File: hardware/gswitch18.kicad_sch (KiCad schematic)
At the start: 21 parts, among them IC1 ATMEGA88P, P1 CONN_6X2, P2 CONN_6X2, P3 CONN_6X2, P4 USB, P5 ISP, X1 12MHz

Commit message: v1.2 KiCAD 6 final changes
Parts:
- removed C2: 22u, symbol gswitch18-rescue:CAPAPOL
- added C1: 0u1, Capacitor_SMD:C_0603_1608Metric, symbol gswitch18-rescue:C
- added C5: (no value), symbol gswitch18-rescue:CAPAPOL
- added MH1, MH2, MH3, MH4: (no value), symbol Mechanical:MountingHole
- C2: renamed from C1; footprint (none) -> Capacitor_SMD:C_0603_1608Metric
- C3, C4: footprint (none) -> Capacitor_SMD:C_0603_1608Metric
- D1: footprint (none) -> Diode_SMD:D_SOD-523
- D2: value Sctky -> (none)
- D3, D4: value 3.6v Zen -> (none); footprint (none) -> Capacitor_SMD:C_1206_3216Metric_Pad1.33x1.80mm_HandSolder
- P1, P2, P3: footprint (none) -> pin_array_6x2
- P4: footprint (none) -> USB-B_mini
- P5: footprint (none) -> pin_array_3x2
- R1, R2, R3, R5, R6, R7: footprint (none) -> Resistor_SMD:R_0603_1608Metric
- U1: renamed from IC1; footprint (none) -> Package_QFP:TQFP-32_7x7mm_P0.8mm
- X1: footprint (none) -> HC-49V
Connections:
- net +5V: now also C1.1, C5.1
- net GND: now also D1.2 (A), D2.2 (A), C1.2, C5.2; no longer D1.1 (A), D2.1 (A)
- net at D3.2 (K), R2.1, R3.2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: now also D2.1 (K); no longer D2.2 (K)
- net at D4.2 (K), R1.1, R5.2: now also D1.1 (K); no longer D1.2 (K)
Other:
- moved on the sheet: C2, D1, D2, D3, D4, R1, R2, R3, R5, R6

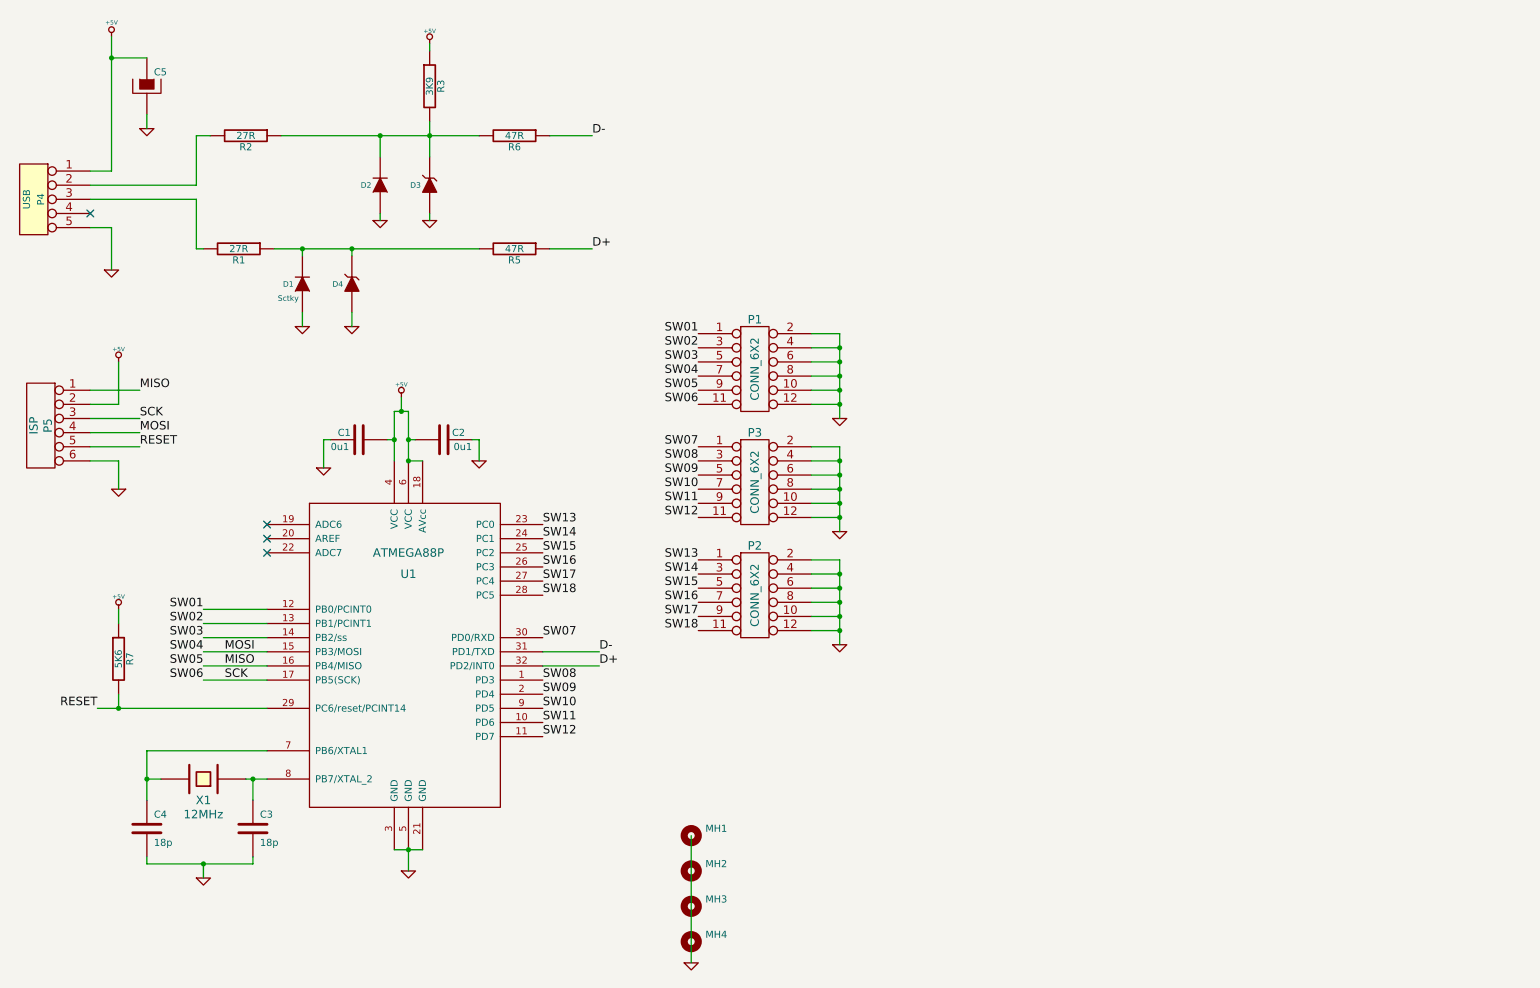
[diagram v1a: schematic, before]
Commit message: Futzing with fully SMD version. Don't like the JST PA connectors.
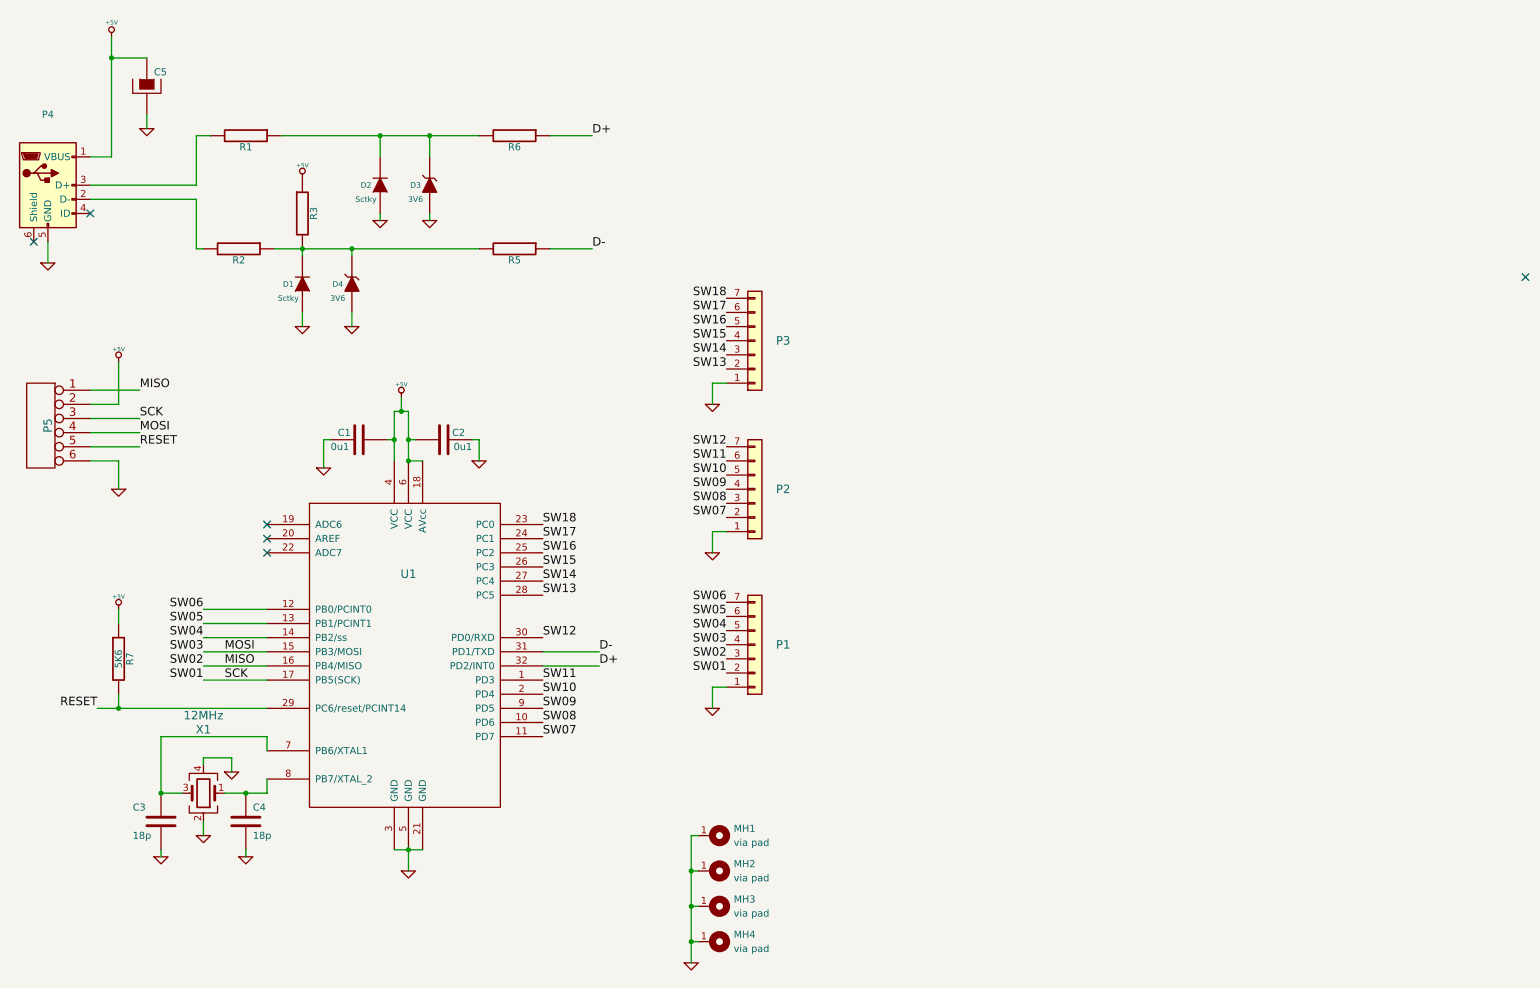
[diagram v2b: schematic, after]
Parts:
- removed P2, P3: CONN_6X2, pin_array_6x2, symbol gswitch18-rescue:CONN_6X2
- removed P4: USB, USB-B_mini, symbol gswitch18-rescue:CONN_5
- added P2, P3: (no value), symbol Connector_Generic:Conn_01x07
- added P4: (no value), symbol Connector:USB_B_Mini
- C5: JLCPCB (none) -> C128254
- D1: JLCPSB (none) -> C122862
- D2: value (none) -> Sctky; footprint (none) -> Diode_SMD:D_SOD-523; JLCPCB (none) -> C122862
- D3, D4: value (none) -> 3V6; footprint Capacitor_SMD:C_1206_3216Metric_Pad1.33x1.80mm_HandSolder -> Diode_SMD:D_SOD-123; JLCPCB (none) -> C8057
- MH1, MH2, MH3, MH4: value (none) -> via pad; footprint (none) -> MountingHole:MountingHole_3.2mm_M3_Pad_Via
- P1: value CONN_6X2 -> (none); footprint pin_array_6x2 -> (none); symbol gswitch18-rescue:CONN_6X2 -> Connector_Generic:Conn_01x07; JLCPCB (none) -> C519164
- P5: value ISP -> (none); footprint pin_array_3x2 -> (none); now left out of the parts list
- R1: renamed from R2; value 27R -> (none); footprint Resistor_SMD:R_0603_1608Metric -> (none); JLCPCB (none) -> C137753
- R2: renamed from R1; value 27R -> (none); footprint Resistor_SMD:R_0603_1608Metric -> (none); JLCPCB (none) -> C137753
- R3: value 3K9 -> (none); footprint Resistor_SMD:R_0603_1608Metric -> (none); JLCPCB (none) -> C137629
- R5, R6: value 47R -> (none); footprint Resistor_SMD:R_0603_1608Metric -> (none); JLCPCB (none) -> C114623
- U1: value ATMEGA88P -> (none); footprint Package_QFP:TQFP-32_7x7mm_P0.8mm -> (none); JLCPCB (none) -> C8727
- X1: footprint HC-49V -> Crystal:Crystal_SMD_3225-4Pin_3.2x2.5mm; symbol gswitch18-rescue:CRYSTAL -> Device:Crystal_GND24; JLCPCB (none) -> C258939
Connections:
- net +5V: now also P4.1 (VBUS)
- net D+: now also R6.1; no longer R5.1
- net D-: now also R5.1; no longer R6.1
- net GND: now also D1.1 (A), D2.1 (A), MH1.1 (G), MH2.1 (G), MH3.1 (G), MH4.1 (G), P1.1 (Pin_1), X1.2, X1.4, P2.1 (Pin_1), P3.1 (Pin_1), P4.5 (GND); no longer D1.2 (A), D2.2 (A), P1.10, P1.12, P1.2 (P2), P1.4 (P4), P1.6 (P6), P1.8 (P8)
- net MISO: now also P1.3 (Pin_3); no longer P1.9
- net MOSI: now also P1.4 (Pin_4); no longer P1.7 (P7)
- net SCK: now also P1.2 (Pin_2); no longer P1.11
- net SW07: now also U1.11 (PD7), P2.2 (Pin_2); no longer U1.30 (PD0/RXD)
- net SW08: now also U1.10 (PD6), P2.3 (Pin_3); no longer U1.1 (PD3)
- net SW09: now also U1.9 (PD5), P2.4 (Pin_4); no longer U1.2 (PD4)
- net SW10: now also U1.2 (PD4), P2.5 (Pin_5); no longer U1.9 (PD5)
- net SW11: now also U1.1 (PD3), P2.6 (Pin_6); no longer U1.10 (PD6)
- net SW12: now also U1.30 (PD0/RXD), P2.7 (Pin_7); no longer U1.11 (PD7)
- net SW13: now also U1.28 (PC5), P3.2 (Pin_2); no longer U1.23 (PC0)
- net SW14: now also U1.27 (PC4), P3.3 (Pin_3); no longer U1.24 (PC1)
- net SW15: now also U1.26 (PC3), P3.4 (Pin_4); no longer U1.25 (PC2)
- net SW16: now also U1.25 (PC2), P3.5 (Pin_5); no longer U1.26 (PC3)
- net SW17: now also U1.24 (PC1), P3.6 (Pin_6); no longer U1.27 (PC4)
- net SW18: now also U1.23 (PC0), P3.7 (Pin_7); no longer U1.28 (PC5)
- net at D3.2 (K), R1.1, R6.2: now also D2.2 (K); no longer D2.1 (K), R3.2
- net at R1.2: now also P4.3 (D+)
- net at D4.2 (K), R2.1, R5.2: now also D1.2 (K), R3.2; no longer D1.1 (K)
- net at R2.2: now also P4.2 (D-)
- net at U1.8 (PB7/XTAL_2), X1.1: now also C4.1; no longer C3.1
- net SW01 renamed SW06
- net SW06: now also P1.7 (Pin_7); no longer P1.1 (P1)
- net SW02 renamed SW05
- net SW05: now also P1.6 (Pin_6); no longer P1.3 (P3)
- net SW03 renamed SW04
- new net: C3.1, U1.7 (PB6/XTAL1), X1.3
- no-connect marks 4 -> 6
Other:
- moved on the sheet: C3, C4, R3

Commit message: smd milestone
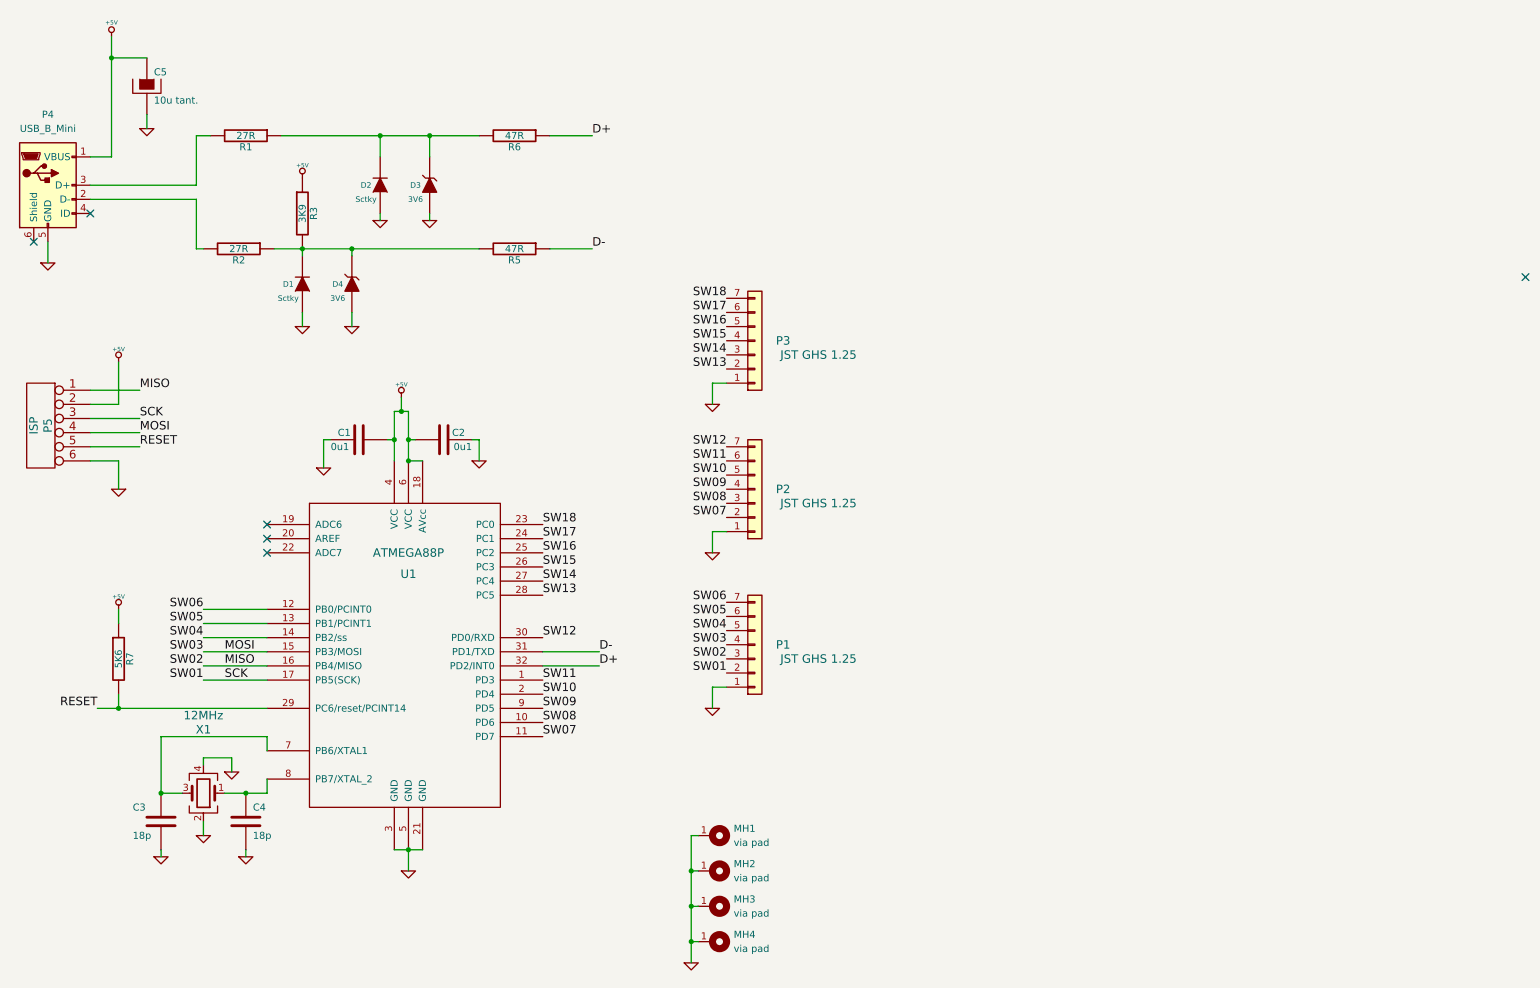
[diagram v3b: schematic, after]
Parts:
- C5: value (none) -> 10u tant.; footprint (none) -> Capacitor_SMD:C_1206_3216Metric
- P1, P2, P3: value (none) -> JST GHS 1.25; footprint (none) -> Connector_JST:JST_GH_BM07B-GHS-TBT_1x07-1MP_P1.25mm_Vertical
- P4: value (none) -> USB_B_Mini; footprint (none) -> Connector_USB:USB_Mini-B_Wuerth_65100516121_Horizontal
- P5: value (none) -> ISP; footprint (none) -> pin_array_3x2
- R1, R2: value (none) -> 27R; footprint (none) -> Resistor_SMD:R_0603_1608Metric
- R3: value (none) -> 3K9; footprint (none) -> Resistor_SMD:R_0603_1608Metric
- R5, R6: value (none) -> 47R; footprint (none) -> Resistor_SMD:R_0603_1608Metric
- U1: value (none) -> ATMEGA88P; footprint (none) -> Package_QFP:TQFP-32_7x7mm_P0.8mm

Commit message: SMD: All JLCPCB part codes loaded. Other fixes.
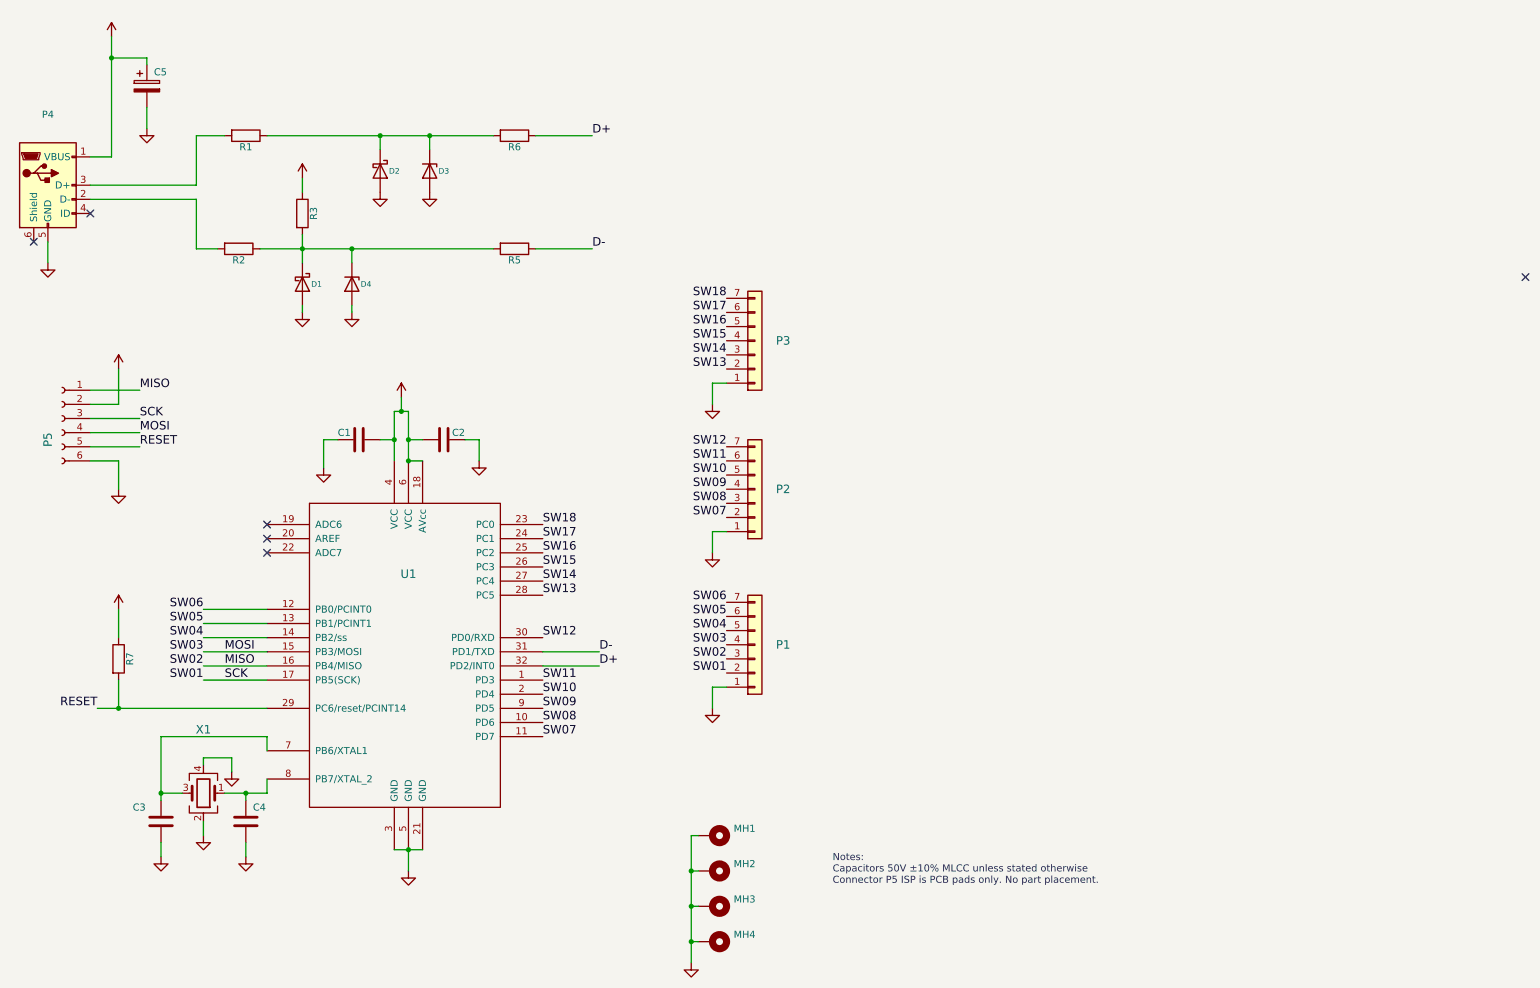
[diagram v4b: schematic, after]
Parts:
- removed MH1, MH2, MH3, MH4: via pad, MountingHole:MountingHole_3.2mm_M3_Pad_Via, symbol Mechanical:MountingHole
- added MH1, MH2, MH3, MH4: (no value), symbol Mechanical:MountingHole_Pad
- C1, C2: value 0u1 -> (none); footprint Capacitor_SMD:C_0603_1608Metric -> (none); symbol gswitch18-rescue:C -> Device:C; JLCPCB (none) -> C14663
- C3, C4: value 18p -> (none); footprint Capacitor_SMD:C_0603_1608Metric -> (none); symbol gswitch18-rescue:C -> Device:C; JLCPCB (none) -> C107040
- C5: value 10u tant. -> (none); footprint Capacitor_SMD:C_1206_3216Metric -> (none); symbol gswitch18-rescue:CAPAPOL -> Device:C_Polarized
- D1: value Sctky -> (none); footprint Diode_SMD:D_SOD-523 -> (none); symbol gswitch18-rescue:DIODE -> Device:D_Schottky; JLCPCB (none) -> C122862; JLCPSB C122862 -> (none)
- D2: value Sctky -> (none); footprint Diode_SMD:D_SOD-523 -> (none); symbol gswitch18-rescue:DIODE -> Device:D_Schottky
- D3, D4: value 3V6 -> (none); footprint Diode_SMD:D_SOD-123 -> (none); symbol gswitch18-rescue:ZENER -> Device:D_Zener; JLCPCB C8057 -> C216708
- P1, P2, P3: value JST GHS 1.25 -> (none); footprint Connector_JST:JST_GH_BM07B-GHS-TBT_1x07-1MP_P1.25mm_Vertical -> (none)
- P4: value USB_B_Mini -> (none); footprint Connector_USB:USB_Mini-B_Wuerth_65100516121_Horizontal -> (none)
- P5: value ISP -> (none); footprint pin_array_3x2 -> (none); symbol gswitch18-rescue:CONN_6 -> Connector:Conn_01x06_Female
- R1, R2: value 27R -> (none); footprint Resistor_SMD:R_0603_1608Metric -> (none); symbol gswitch18-rescue:R -> Device:R
- R3: value 3K9 -> (none); footprint Resistor_SMD:R_0603_1608Metric -> (none); symbol gswitch18-rescue:R -> Device:R; JLCPCB C137629 -> C114616
- R5, R6: value 47R -> (none); footprint Resistor_SMD:R_0603_1608Metric -> (none); symbol gswitch18-rescue:R -> Device:R
- R7: value 5K6 -> (none); footprint Resistor_SMD:R_0603_1608Metric -> (none); symbol gswitch18-rescue:R -> Device:R; JLCPCB (none) -> C114627
- U1: value ATMEGA88P -> (none); footprint Package_QFP:TQFP-32_7x7mm_P0.8mm -> (none)
- X1: value 12MHz -> (none); footprint Crystal:Crystal_SMD_3225-4Pin_3.2x2.5mm -> (none)
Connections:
- net GND: now also D1.2 (A), D2.2 (A), D3.2 (A), D4.2 (A), MH1.1, MH2.1, MH3.1, MH4.1; no longer D1.1 (A), D2.1 (A), D3.1 (A), D4.1 (A)
- net at R1.1, R6.2: now also D2.1 (K), D3.1 (K); no longer D2.2 (K), D3.2 (K)
- net at R2.1, R3.2, R5.2: now also D1.1 (K), D4.1 (K); no longer D1.2 (K), D4.2 (K)
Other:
- note added: "Notes: Capacitors 50V ±10% MLCC unless stated otherwise Connector P5 ISP is PCB pads only. No part placement."
- moved on the sheet: D1, D2, D3, D4
